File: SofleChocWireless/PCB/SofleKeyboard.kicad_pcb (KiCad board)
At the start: 2 copper layers, 143.4 x 111.8 mm, 85 parts, among them J3 OLED, SW1 SW_PUSH_LED, SW10 SW_PUSH_LED, SW11 SW_PUSH_LED, SW12 SW_PUSH_LED, SW13 SW_PUSH_LED, SW14 SW_PUSH_LED, SW15 SW_PUSH_LED, SW16 SW_PUSH_LED, SW17 SW_PUSH_LED, SW18 SW_PUSH_LED, SW19 SW_PUSH_LED, SW2 SW_PUSH_LED, SW20 SW_PUSH_LED, SW21 SW_PUSH_LED, SW22 SW_PUSH_LED, SW23 SW_PUSH_LED, SW24 SW_PUSH_LED, SW25 SW_PUSH_LED, SW26 SW_PUSH_LED, SW27 SW_PUSH_LED, SW28 SW_PUSH_LED, SW29 SW_PUSH_LED, SW3 SW_PUSH_LED, SW30 SW_PUSH_LED, SW31 Rotary_Encoder_Switch, SW4 SW_PUSH_LED, SW5 SW_PUSH_LED, SW6 SW_PUSH_LED, SW7 SW_PUSH_LED, SW8 SW_PUSH_LED, SW9 SW_PUSH_LED, U1 ProMicro

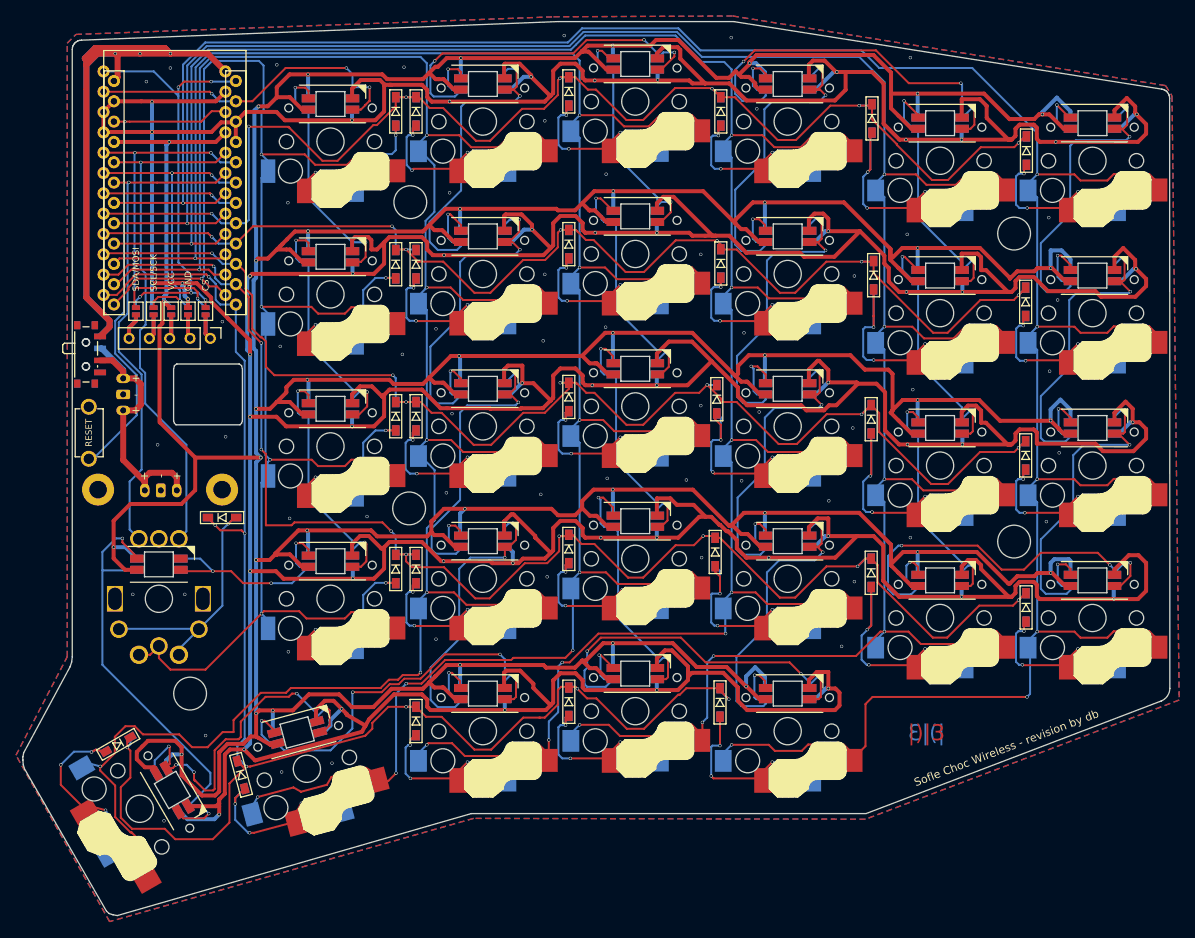
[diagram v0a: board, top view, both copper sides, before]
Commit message: Add support for PG1353 and PG1353s
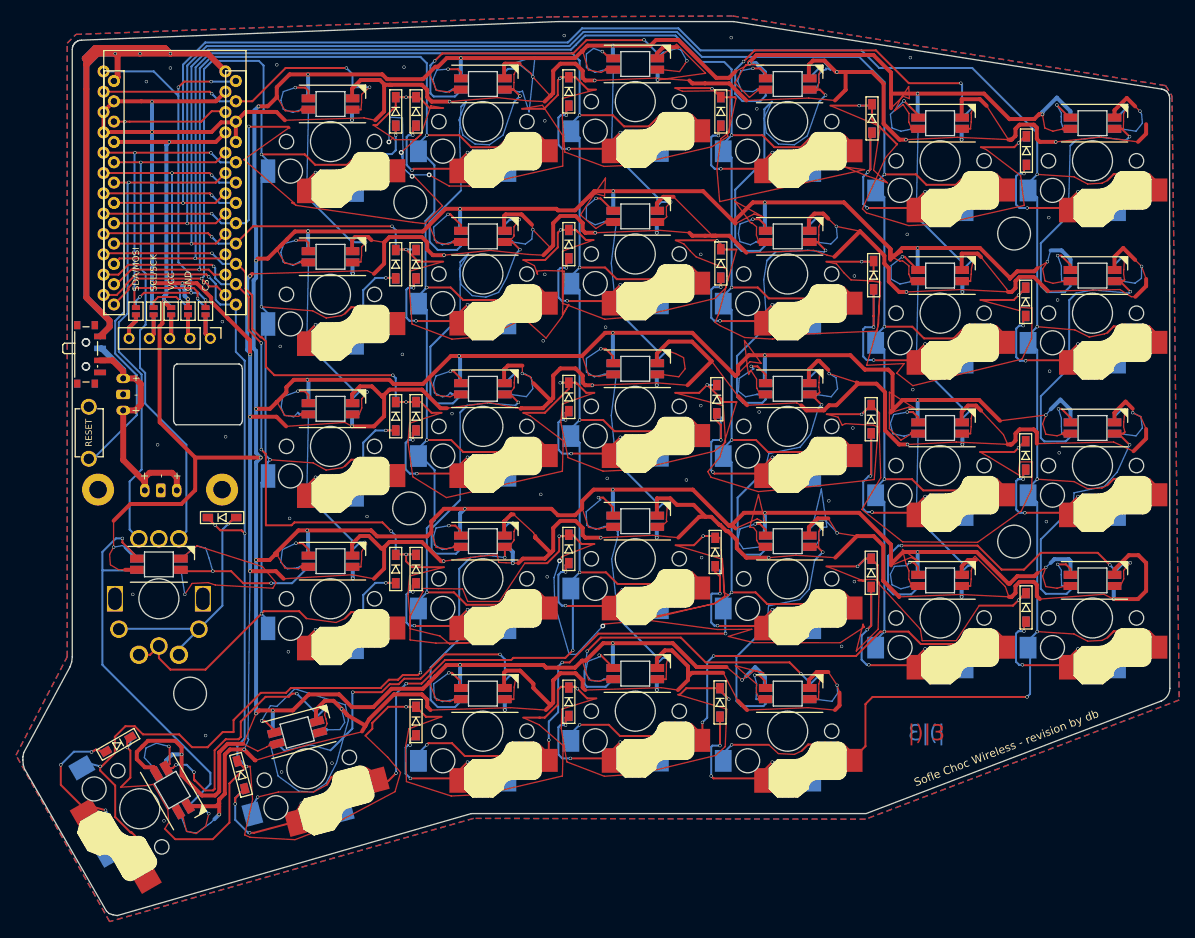
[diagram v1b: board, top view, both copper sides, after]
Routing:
- net row0: track 164.2 -> 338.7 mm, vias 7 -> 11
- net row3: track 183.3 -> 319.4 mm, vias 9 -> 11
- net row1: track 148.8 -> 273.8 mm
- net row2: track 162.1 -> 279.9 mm
- net VCC: track 959.1 -> 1068.2 mm
- net GND: track 1120.8 -> 1208.8 mm, vias 107 -> 98
- net row4: track 202.2 -> 282.4 mm
- net Net-(SW27-Pad2): track 53.2 -> 84.4 mm
- net Net-(SW14-Pad2): track 46.5 -> 59.0 mm
- net Net-(SW10-Pad2): track 47.1 -> 58.9 mm
- net Net-(SW2-Pad4): track 47.6 -> 58.9 mm
- net Net-(SW2-Pad2): track 51.2 -> 58.2 mm
- net Net-(SW15-Pad4): track 33.2 -> 39.3 mm
- net Net-(SW19-Pad2): track 29.0 -> 34.2 mm
- net Net-(SW17-Pad2): track 31.6 -> 35.4 mm
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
